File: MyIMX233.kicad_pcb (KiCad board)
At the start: 2 copper layers, 74.1 x 92 mm, 101 parts, among them IC1 iMX233, IC2 DDR_SDRAM_MT46_x16, J1 USB_OTG, J2 CONN_01X01, P1 4p2, P2 1v2, P3 VDDA1v8, P4 2v5, P5 3v3, P6 1v, SW1 SWITCH_PUSHBUTTON, Y1 24Mhz

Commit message: kicad removed unconnected wire and added bill of materials plus some images in kitsnspares
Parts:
- moved C25 0.80 mm to (119.2, 89.7)
- moved D2 0.71 mm to (124.9, 81.0)
- moved R26 0.55 mm to (119.0, 91.4)
- moved C42 0.13 mm to (121.5, 85.9)
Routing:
- net Net-(IC1-Pad91): track 50.9 -> 48.6 mm
- net /+VE: track 67.5 -> 67.0 mm
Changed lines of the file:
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@@
-(kicad_pcb (version 20170123) (host pcbnew "(2017-06-28 revision 2237de015)-makepkg")
+(kicad_pcb (version 20170123) (host pcbnew "(2017-08-16 revision 90873a101)-makepkg")
   (general
     (thickness 1.6)
@@
   )
   (module Capacitors_THT:CP_Radial_D5.0mm_P2.50mm (layer F.Cu)
-    (at 121.5136 86.0044)
+    (at 121.4901 85.8774)
     (descr "CP, Radial series, Radial, pin pitch=2.50mm, , diameter=5mm, Electrolytic Capacitor")
     (tags "CP Radial series Radial pin pitch 2.50mm  diameter 5mm Electrolytic Capacitor")
@@
   )
   (module Resistors_SMD:R_0603_HandSoldering (layer F.Cu)
-    (at 119.38 91.0844 180)
+    (at 118.9658 91.44 180)
     (descr "Resistor SMD 0603, hand soldering")
     (tags "resistor 0603")
@@
   )
   (module Diodes_SMD:D_SOD-323_HandSoldering (layer F.Cu)
-    (at 124.7775 81.7045 90)
+    (at 124.8918 81.0079 90)
     (descr SOD-323)
     (tags SOD-323)
@@
   )
   (module Capacitors_SMD:C_0805_HandSoldering (layer F.Cu)
-    (at 119.7048 89.1032 180)
+    (at 119.1968 89.7255 180)
     (descr "Capacitor SMD 0805, hand soldering")
     (tags "capacitor 0805")
@@
   (via (at 124.7648 117.7036) (size 0.45) (drill 0.15) (layers F.Cu B.Cu) (net 114))
   (segment (start 122.428 117.725) (end 123.355 117.725) (width 0.127) (layer F.Cu) (net 114))
+  (segment (start 123.7996 77.419212) (end 124.7775 78.397112) (width 0.3) (layer F.Cu) (net 115))
+  (segment (start 124.7775 78.397112) (end 124.7775 79.9338) (width 0.3) (layer F.Cu) (net 115))
   (segment (start 124.024599 77.194213) (end 123.7996 77.419212) (width 0.3) (layer B.Cu) (net 115))
   (segment (start 129.286 77.1525) (end 124.066312 77.1525) (width 0.3) (layer B.Cu) (net 115))
@@
   (segment (start 124.066312 77.1525) (end 124.024599 77.194213) (width 0.3) (layer B.Cu) (net 115))
   (segment (start 126.619 68.58) (end 123.7996 71.3994) (width 0.3) (layer F.Cu) (net 115))
-  (segment (start 124.7775 78.397112) (end 124.024599 77.644211) (width 0.3) (layer F.Cu) (net 115))
-  (segment (start 124.7775 80.4545) (end 124.7775 78.397112) (width 0.3) (layer F.Cu) (net 115))
   (segment (start 123.748788 77.419212) (end 123.7996 77.419212) (width 0.3) (layer B.Cu) (net 115))
   (segment (start 118.11 83.058) (end 123.748788 77.419212) (width 0.3) (layer B.Cu) (net 115))
-  (segment (start 124.024599 77.644211) (end 123.7996 77.419212) (width 0.3) (layer F.Cu) (net 115))
   (via (at 123.7996 77.419212) (size 0.45) (drill 0.15) (layers F.Cu B.Cu) (net 115))
   (segment (start 133.1595 53.721) (end 133.1595 58.781) (width 0.3) (layer F.Cu) (net 115))
@@
   (segment (start 126.619 71.12) (end 126.619 72.898) (width 0.3) (layer F.Cu) (net 128))
   (segment (start 126.619 72.898) (end 127.254 73.533) (width 0.3) (layer F.Cu) (net 128))
-  (segment (start 114.5032 90.806) (end 114.2248 91.0844) (width 0.3) (layer F.Cu) (net 129))
+  (segment (start 122.3547 82.9535) (end 122.8598 82.4484) (width 0.3) (layer F.Cu) (net 129))
+  (segment (start 122.8598 82.4484) (end 124.8791 82.4484) (width 0.3) (layer F.Cu) (net 129))
+  (segment (start 122.3547 82.9545) (end 122.3547 82.9535) (width 0.3) (layer F.Cu) (net 129))
+  (segment (start 126.873 82.677) (end 124.968 82.677) (width 0.3) (layer F.Cu) (net 129))
+  (segment (start 124.968 82.677) (end 124.8029 82.5119) (width 0.3) (layer F.Cu) (net 129))
+  (segment (start 114.2248 91.0844) (end 122.3547 82.9545) (width 0.3) (layer F.Cu) (net 129))
   (segment (start 114.2248 91.0844) (end 113.4032 91.906) (width 0.3) (layer F.Cu) (net 129))
   (segment (start 114.7816 91.0844) (end 114.2248 91.0844) (width 0.3) (layer F.Cu) (net 129))
-  (segment (start 122.3547 82.9545) (end 114.5032 90.806) (width 0.3) (layer F.Cu) (net 129))
   (segment (start 114.7816 91.0844) (end 118.28 91.0844) (width 0.3) (layer F.Cu) (net 129))
   (segment (start 113.4032 92.456) (end 113.4032 93.5013) (width 0.3) (layer F.Cu) (net 129))
   (segment (start 113.4032 93.5013) (end 113.369 93.5355) (width 0.3) (layer F.Cu) (net 129))
-  (segment (start 124.7775 82.9545) (end 122.3547 82.9545) (width 0.3) (layer F.Cu) (net 129))
   (segment (start 113.4032 91.906) (end 113.4032 92.456) (width 0.3) (layer F.Cu) (net 129))
   (segment (start 132.0165 68.6435) (end 134.8105 68.6435) (width 0.3) (layer B.Cu) (net 129))
@@
   (segment (start 137.795 79.3575) (end 137.1425 80.01) (width 0.3) (layer B.Cu) (net 129))
   (segment (start 134.8105 68.6435) (end 137.795 71.628) (width 0.3) (layer B.Cu) (net 129))
-  (segment (start 124.7775 82.9545) (end 126.5955 82.9545) (width 0.3) (layer F.Cu) (net 129))
-  (segment (start 126.873 82.677) (end 126.5955 82.9545) (width 0.3) (layer F.Cu) (net 129))
   (segment (start 105.693663 96.709219) (end 106.933405 95.469477) (width 0.127) (layer F.Cu) (net 129))
   (segment (start 106.933405 95.469477) (end 108.639472 95.469477) (width 0.127) (layer F.Cu) (net 129))
@@
   (segment (start 103.038724 72.644) (end 104.013 71.669724) (width 0.127) (layer B.Cu) (net 88))
   (segment (start 104.013 71.669724) (end 104.013 69.4055) (width 0.127) (layer B.Cu) (net 88))
-  (segment (start 95.0595 81.258224) (end 95.0595 83.566) (width 0.127) (layer B.Cu) (net 88))
   (segment (start 104.013 69.4055) (end 106.469 66.9495) (width 0.127) (layer F.Cu) (net 88))
   (segment (start 106.469 66.9495) (end 106.8705 66.9495) (width 0.127) (layer F.Cu) (net 88))
@@
   (segment (start 125.73 58.109) (end 125.265 57.644) (width 0.4) (layer F.Cu) (net 131))
   (segment (start 125.265 57.644) (end 125.265 57.4675) (width 0.4) (layer F.Cu) (net 131))
-  (segment (start 120.48 91.0844) (end 120.48 90.762) (width 0.3) (layer F.Cu) (net 132))
-  (segment (start 119.888 90.17) (end 119.126 90.17) (width 0.3) (layer F.Cu) (net 132))
-  (segment (start 120.48 90.762) (end 119.888 90.17) (width 0.3) (layer F.Cu) (net 132))
-  (segment (start 119.126 90.17) (end 118.4548 89.4988) (width 0.3) (layer F.Cu) (net 132))
-  (segment (start 118.4548 89.4988) (end 118.4548 89.1032) (width 0.3) (layer F.Cu) (net 132))
-  (segment (start 118.4548 89.1032) (end 118.4548 88.9108) (width 0.3) (layer F.Cu) (net 132))
-  (segment (start 118.4548 88.9108) (end 121.3612 86.0044) (width 0.3) (layer F.Cu) (net 132))
-  (segment (start 121.3612 86.0044) (end 121.5136 86.0044) (width 0.3) (layer F.Cu) (net 132))
+  (segment (start 117.9703 89.7636) (end 119.5832 91.3765) (width 0.3) (layer F.Cu) (net 132))
+  (segment (start 119.5832 91.3765) (end 120.015 91.3765) (width 0.3) (layer F.Cu) (net 132))
+  (segment (start 120.1674 91.3638) (end 120.1674 91.3765) (width 0.3) (layer F.Cu) (net 132))
+  (segment (start 120.1674 91.3765) (end 120.1166 91.4273) (width 0.3) (layer F.Cu) (net 132))
+  (segment (start 117.9468 89.7255) (end 118.0718 89.7255) (width 0.127) (layer F.Cu) (net 132))
+  (segment (start 119.6085 91.2622) (end 120.0404 91.2622) (width 0.127) (layer F.Cu) (net 132))
+  (segment (start 121.5136 86.0044) (end 121.3612 86.0044) (width 0.3) (layer F.Cu) (net 132))
+  (segment (start 121.3612 86.0044) (end 118.4548 88.9108) (width 0.3) (layer F.Cu) (net 132))
+  (segment (start 118.4548 88.9108) (end 118.4548 89.4988) (width 0.3) (layer F.Cu) (net 132))
   (segment (start 135.593 61.4045) (end 135.593 63.5586) (width 0.3) (layer F.Cu) (net 133))
   (segment (start 135.593 63.5586) (end 135.8392 63.8048) (width 0.3) (layer F.Cu) (net 133))

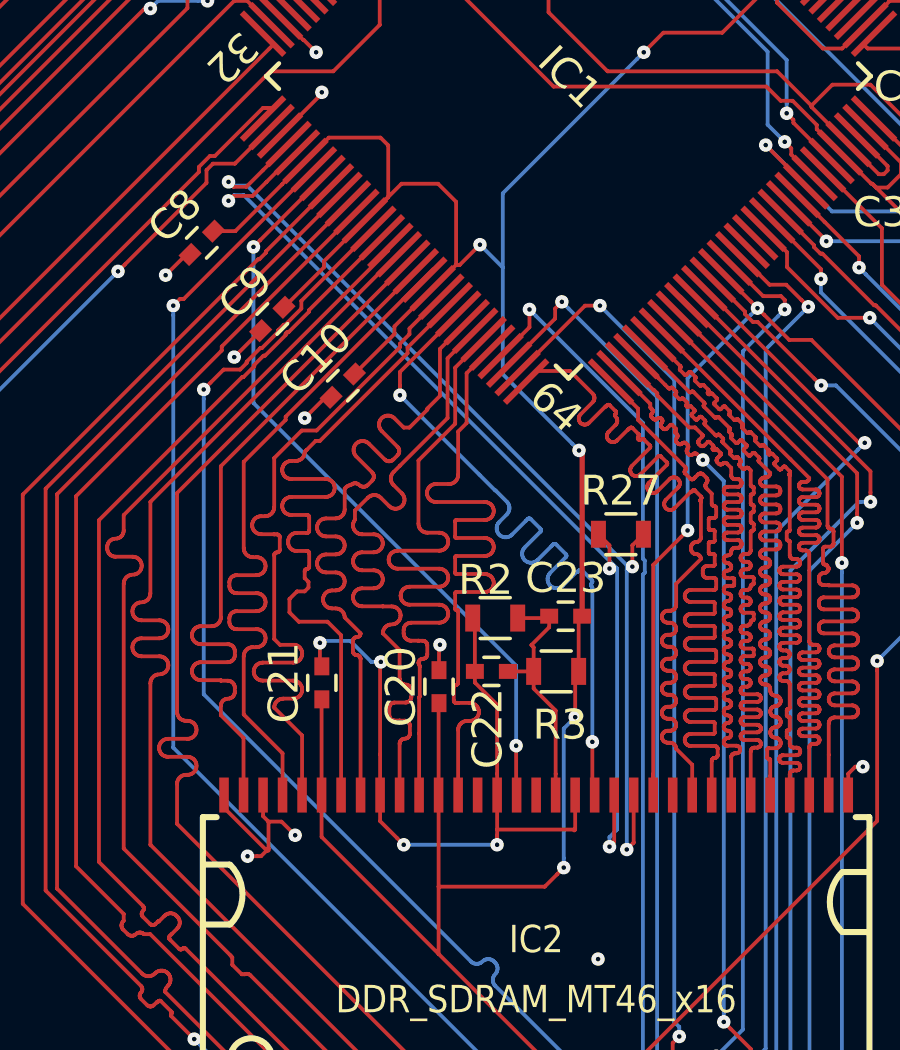
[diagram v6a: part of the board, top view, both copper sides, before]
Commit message: clk nclk termination resistor position fixed and due to which some more length tuning of udq udm
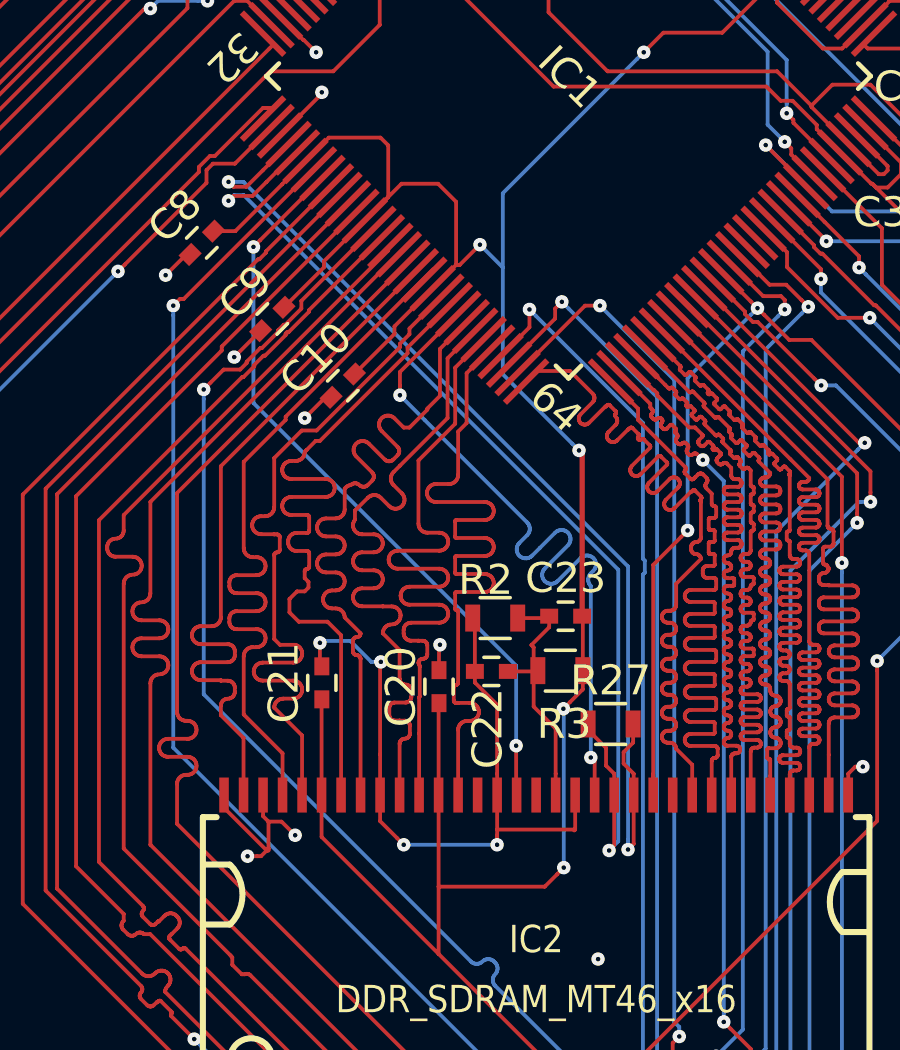
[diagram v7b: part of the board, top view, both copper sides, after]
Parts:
- moved R27 6.33 mm to (98.4, 120.5)
- moved R3 0.14 mm to (96.7, 118.7)
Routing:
- net /CK-: track 33.8 -> 35.2 mm, vias 3 -> 2
- net /CK+: track 34.1 -> 35.2 mm, vias 3 -> 2
